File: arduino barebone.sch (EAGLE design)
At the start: 20 parts

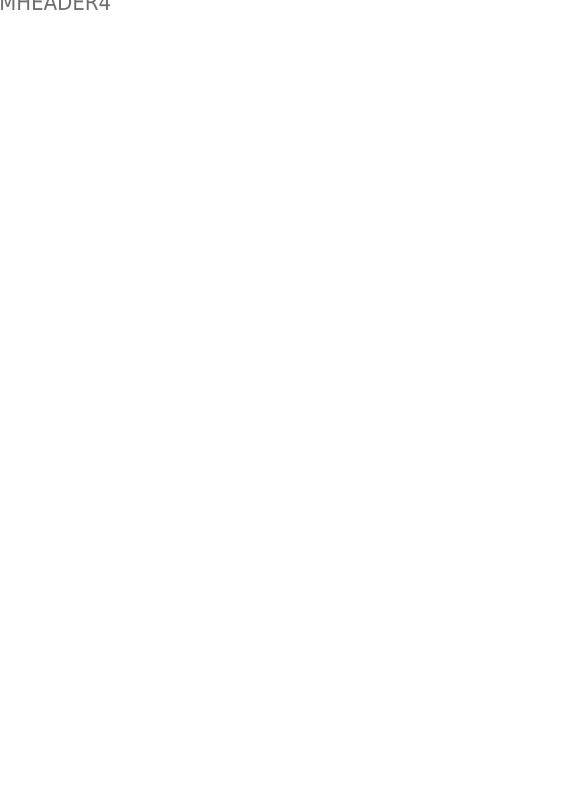
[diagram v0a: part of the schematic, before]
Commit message: started placing components. arduino shield layout
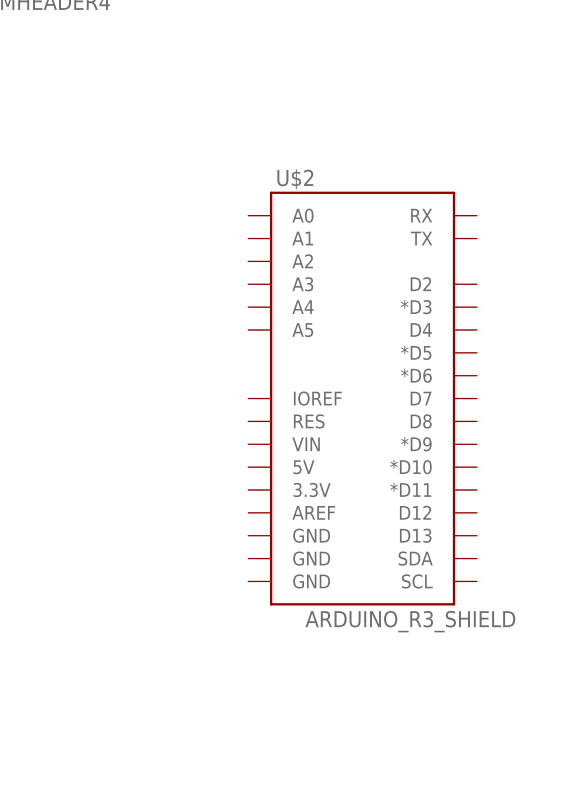
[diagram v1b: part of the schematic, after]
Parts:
- added U$2: ARDUINO_R3_SHIELD, SparkFun-Boards:ARDUINO_R3_SHIELD
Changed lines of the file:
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@@
 <part name="P+3" library="supply1" deviceset="+5V" device=""/>
 <part name="GND9" library="supply1" deviceset="GND" device=""/>
+<part name="U$2" library="SparkFun-Boards" deviceset="ARDUINO_R3_SHIELD" device=""/>
 </parts>
 <sheets>
@@
 <instance part="P+3" gate="1" x="-58.42" y="-73.66"/>
 <instance part="GND9" gate="1" x="-43.18" y="-78.74"/>
+<instance part="U$2" gate="G$1" x="160.02" y="-22.86"/>
 </instances>
 <busses>
